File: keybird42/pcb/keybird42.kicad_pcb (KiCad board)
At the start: 2 copper layers, 180 parts, among them SW111 SW_MX, SW112 SW_MX, SW113 SW_MX, SW114 SW_MX, SW115 SW_MX, SW116 SW_MX, SW117 SW_MX, SW121 SW_MX, SW122 SW_MX, SW123 SW_MX, SW124 SW_MX, SW125 SW_MX, SW126 SW_MX, SW127 SW_MX, SW131 SW_MX, SW132 SW_MX, SW133 SW_MX, SW134 SW_MX, SW135 SW_MX, SW136 SW_MX, SW137 SW_MX, SW211 SW_MX, SW212 SW_MX, SW213 SW_MX, SW214 SW_MX, SW215 SW_MX, SW216 SW_MX, SW217 SW_MX, SW221 SW_MX, SW222 SW_MX, SW223 SW_MX, SW225 SW_MX, SW226 SW_MX, SW227 SW_MX, SW231 SW_MX, SW232 SW_MX, SW233 SW_MX, SW234 SW_MX, SW235 SW_MX, SW236 SW_MX, SW237 SW_MX, SW311 SW_MX, SW312 SW_MX, SW313 SW_MX, SW314 SW_MX, SW315 SW_MX, SW316 SW_MX, SW317 SW_MX, SW321 SW_MX, SW322 SW_MX, SW323 SW_MX, SW324 SW_MX, SW325 SW_MX, SW326 SW_MX, SW327 SW_MX, SW331 SW_MX, SW332 SW_MX, SW333 SW_MX, SW334 SW_MX, SW335 SW_MX, SW336 SW_MX, SW337 SW_MX, SW411 SW_MX, SW412 SW_MX, SW413 SW_MX, SW414 SW_MX, SW415 SW_MX, SW416 SW_MX, SW417 SW_MX, SW421 SW_MX, SW422 SW_MX, SW423 SW_MX, SW424 SW_MX, SW425 SW_MX, SW426 SW_MX, SW427 SW_MX, SW431 SW_MX, SW432 SW_MX, SW433 SW_MX, SW434 SW_MX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

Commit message: row 3, two more gaps
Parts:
- removed D313, D326: 1N4148W, Diode_SMD:D_SOD-123
- removed SW313, SW326: SW_MX, PCM_Switch_Keyboard_Hotswap_Kailh:SW_Hotswap_Kailh_MX
- moved SW327 307.4 mm to (406.4, 76.2)
- moved SW316 297.2 mm to (322.6, 63.5)
- moved SW337 283.5 mm to (425.4, 76.2)
- moved SW317 257.9 mm to (387.4, 76.2)
- moved SW315 247.7 mm to (265.4, 63.5)
- moved SW334 240.8 mm to (246.4, 63.5)
- moved SW336 207.5 mm to (348.0, 63.5)
- moved SW333 204.3 mm to (189.2, 63.5)
- moved SW314 203.6 mm to (208.3, 63.5)
- moved SW325 193.7 mm to (284.5, 63.5)
- moved SW332 181.4 mm to (151.1, 63.5)
- moved SW331 163.8 mm to (69.8, 76.2)
- moved SW335 160.5 mm to (303.5, 63.5)
- moved SW312 149.2 mm to (109.2, 63.5)
- moved SW311 146.1 mm to (31.8, 76.2)
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
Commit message: rough positioning of row 4, two more holes
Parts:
- removed D422, D435: 1N4148W, Diode_SMD:D_SOD-123
- removed SW422, SW435: SW_MX, PCM_Switch_Keyboard_Hotswap_Kailh:SW_Hotswap_Kailh_MX
- moved SW437 316.1 mm to (425.4, 95.2)
- moved SW417 281.6 mm to (387.4, 95.2)
- moved SW436 264.4 mm to (361.9, 82.5)
- moved SW427 251.2 mm to (406.4, 95.2)
- moved SW416 219.6 mm to (312.4, 82.5)
- moved SW421 190.8 mm to (50.8, 95.2)
- moved SW426 185.4 mm to (337.8, 82.5)
- moved SW415 181.3 mm to (274.3, 82.5)
- moved SW434 171.2 mm to (255.3, 82.5)
- moved SW425 138.3 mm to (293.4, 82.5)
- moved SW433 134.2 mm to (198.1, 82.5)
- moved SW414 133.8 mm to (217.2, 82.5)
- moved SW411 128.8 mm to (31.8, 95.2)
- moved SW431 128.7 mm to (69.8, 95.2)
- moved SW432 117.1 mm to (141.0, 82.5)
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
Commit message: row 5, no holes, positioning is very sketchy
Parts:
- moved SW507 197.6 mm to (355.6, 101.6)
- moved SW506 167.9 mm to (330.2, 101.6)
- moved SW505 138.2 mm to (304.8, 101.6)
- moved SW501 81.0 mm to (101.6, 101.6)
- moved SW504 67.1 mm to (228.6, 101.6)
- moved SW502 58.3 mm to (127.0, 101.6)
- moved SW503 45.0 mm to (152.4, 101.6)
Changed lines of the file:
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@@
   )
   (footprint "PCM_Switch_Keyboard_Hotswap_Kailh:SW_Hotswap_Kailh_MX" (layer "F.Cu")
-    (at 182.57 134.93)
+    (at 152.4 101.6)
     (descr "Kailh keyswitch Hotswap Socket")
     (tags "Kailh Keyboard Keyswitch Switch Hotswap Socket Relief Cutout")
@@
   )
   (footprint "PCM_Switch_Keyboard_Hotswap_Kailh:SW_Hotswap_Kailh_MX" (layer "F.Cu")
-    (at 182.57 119.38)
+    (at 127 101.6)
     (descr "Kailh keyswitch Hotswap Socket")
     (tags "Kailh Keyboard Keyswitch Switch Hotswap Socket Relief Cutout")
@@
   )
   (footprint "PCM_Switch_Keyboard_Hotswap_Kailh:SW_Hotswap_Kailh_MX" (layer "F.Cu")
-    (at 182.57 150.48)
+    (at 228.6 101.6)
     (descr "Kailh keyswitch Hotswap Socket")
     (tags "Kailh Keyboard Keyswitch Switch Hotswap Socket Relief Cutout")
@@
   )
   (footprint "PCM_Switch_Keyboard_Hotswap_Kailh:SW_Hotswap_Kailh_MX" (layer "F.Cu")
-    (at 182.57 181.58)
+    (at 330.2 101.6)
     (descr "Kailh keyswitch Hotswap Socket")
     (tags "Kailh Keyboard Keyswitch Switch Hotswap Socket Relief Cutout")
@@
   )
   (footprint "PCM_Switch_Keyboard_Hotswap_Kailh:SW_Hotswap_Kailh_MX" (layer "F.Cu")
-    (at 182.57 103.83)
+    (at 101.6 101.6)
     (descr "Kailh keyswitch Hotswap Socket")
     (tags "Kailh Keyboard Keyswitch Switch Hotswap Socket Relief Cutout")
@@
   )
   (footprint "PCM_Switch_Keyboard_Hotswap_Kailh:SW_Hotswap_Kailh_MX" (layer "F.Cu")
-    (at 182.57 197.13)
+    (at 355.6 101.6)
     (descr "Kailh keyswitch Hotswap Socket")
     (tags "Kailh Keyboard Keyswitch Switch Hotswap Socket Relief Cutout")
@@
   )
   (footprint "PCM_Switch_Keyboard_Hotswap_Kailh:SW_Hotswap_Kailh_MX" (layer "F.Cu")
-    (at 182.57 166.03)
+    (at 304.8 101.6)
     (descr "Kailh keyswitch Hotswap Socket")
     (tags "Kailh Keyboard Keyswitch Switch Hotswap Socket Relief Cutout")

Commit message: diodes in roughly the right places
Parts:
- moved D127 279.6 mm to (406.4, 36.8)
- moved D137 275.7 mm to (425.4, 36.8)
- moved D237 273.6 mm to (425.4, 55.9)
- moved D117 249.9 mm to (387.4, 36.8)
- moved D217 249.2 mm to (387.4, 54.6)
- moved D227 245.5 mm to (407.7, 55.9)
- moved D126 239.1 mm to (344.2, 29.2)
- moved D327 238.6 mm to (406.4, 81.3)
- moved D337 237.4 mm to (425.4, 81.3)
- moved D437 234.5 mm to (425.4, 100.3)
- moved D136 228.7 mm to (361.9, 30.5)
- moved D236 223.5 mm to (355.6, 49.5)
- moved D211 221.0 mm to (31.8, 54.6)
- moved D121 215.7 mm to (50.8, 36.8)
- moved D111 212.9 mm to (31.8, 36.8)
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
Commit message: swap pins of switches so that traces to diodes are neater
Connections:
- SW111 pad 1: /COL1 -> Net-(D111-A)
- SW111 pad 2: Net-(D111-A) -> /COL1
- SW112 pad 1: /COL2 -> Net-(D112-A)
- SW112 pad 2: Net-(D112-A) -> /COL2
- SW113 pad 1: /COL3 -> Net-(D113-A)
- SW113 pad 2: Net-(D113-A) -> /COL3
- SW114 pad 1: /COL4 -> Net-(D114-A)
- SW114 pad 2: Net-(D114-A) -> /COL4
- SW115 pad 1: /COL5 -> Net-(D115-A)
- SW115 pad 2: Net-(D115-A) -> /COL5
- SW116 pad 1: /COL6 -> Net-(D116-A)
- SW116 pad 2: Net-(D116-A) -> /COL6
- SW117 pad 1: /COL7 -> Net-(D117-A)
- SW117 pad 2: Net-(D117-A) -> /COL7
- SW121 pad 1: /COL1 -> Net-(D121-A)
- SW121 pad 2: Net-(D121-A) -> /COL1
- SW122 pad 1: /COL2 -> Net-(D122-A)
- SW122 pad 2: Net-(D122-A) -> /COL2
- SW123 pad 1: /COL3 -> Net-(D123-A)
- SW123 pad 2: Net-(D123-A) -> /COL3
- SW124 pad 1: /COL4 -> Net-(D124-A)
- SW124 pad 2: Net-(D124-A) -> /COL4
- SW125 pad 1: /COL5 -> Net-(D125-A)
- SW125 pad 2: Net-(D125-A) -> /COL5
- SW126 pad 1: /COL6 -> Net-(D126-A)
- SW126 pad 2: Net-(D126-A) -> /COL6
- SW127 pad 1: /COL7 -> Net-(D127-A)
- SW127 pad 2: Net-(D127-A) -> /COL7
- SW131 pad 1: /COL1 -> Net-(D131-A)
- SW131 pad 2: Net-(D131-A) -> /COL1
- SW132 pad 1: /COL2 -> Net-(D132-A)
- SW132 pad 2: Net-(D132-A) -> /COL2
- SW133 pad 1: /COL3 -> Net-(D133-A)
- SW133 pad 2: Net-(D133-A) -> /COL3
- SW134 pad 1: /COL4 -> Net-(D134-A)
- SW134 pad 2: Net-(D134-A) -> /COL4
- SW135 pad 1: /COL5 -> Net-(D135-A)
- SW135 pad 2: Net-(D135-A) -> /COL5
- SW136 pad 1: /COL6 -> Net-(D136-A)
- SW136 pad 2: Net-(D136-A) -> /COL6
- SW137 pad 1: /COL7 -> Net-(D137-A)
- SW137 pad 2: Net-(D137-A) -> /COL7
- SW211 pad 1: /COL1 -> Net-(D211-A)
- SW211 pad 2: Net-(D211-A) -> /COL1
- SW212 pad 1: /COL2 -> Net-(D212-A)
- SW212 pad 2: Net-(D212-A) -> /COL2
- SW213 pad 1: /COL3 -> Net-(D213-A)
- SW213 pad 2: Net-(D213-A) -> /COL3
- SW214 pad 1: /COL4 -> Net-(D214-A)
- SW214 pad 2: Net-(D214-A) -> /COL4
- SW215 pad 1: /COL5 -> Net-(D215-A)
- SW215 pad 2: Net-(D215-A) -> /COL5
- SW216 pad 1: /COL6 -> Net-(D216-A)
- SW216 pad 2: Net-(D216-A) -> /COL6
- SW217 pad 1: /COL7 -> Net-(D217-A)
- SW217 pad 2: Net-(D217-A) -> /COL7
- SW221 pad 1: /COL1 -> Net-(D221-A)
- SW221 pad 2: Net-(D221-A) -> /COL1
- SW222 pad 1: /COL2 -> Net-(D222-A)
- SW222 pad 2: Net-(D222-A) -> /COL2
- SW223 pad 1: /COL3 -> Net-(D223-A)
- SW223 pad 2: Net-(D223-A) -> /COL3
- SW225 pad 1: /COL5 -> Net-(D225-A)
- SW225 pad 2: Net-(D225-A) -> /COL5
- SW226 pad 1: /COL6 -> Net-(D226-A)
- SW226 pad 2: Net-(D226-A) -> /COL6
- SW227 pad 1: /COL7 -> Net-(D227-A)
- SW227 pad 2: Net-(D227-A) -> /COL7
- SW231 pad 1: /COL1 -> Net-(D231-A)
- SW231 pad 2: Net-(D231-A) -> /COL1
- SW232 pad 1: /COL2 -> Net-(D232-A)
- SW232 pad 2: Net-(D232-A) -> /COL2
- SW233 pad 1: /COL3 -> Net-(D233-A)
- SW233 pad 2: Net-(D233-A) -> /COL3
- SW234 pad 1: /COL4 -> Net-(D234-A)
- SW234 pad 2: Net-(D234-A) -> /COL4
- SW235 pad 1: /COL5 -> Net-(D235-A)
- SW235 pad 2: Net-(D235-A) -> /COL5
- SW236 pad 1: /COL6 -> Net-(D236-A)
- SW236 pad 2: Net-(D236-A) -> /COL6
- SW237 pad 1: /COL7 -> Net-(D237-A)
- SW237 pad 2: Net-(D237-A) -> /COL7
- SW311 pad 1: /COL1 -> Net-(D311-A)
- SW311 pad 2: Net-(D311-A) -> /COL1
- SW312 pad 1: /COL2 -> Net-(D312-A)
- SW312 pad 2: Net-(D312-A) -> /COL2
- SW314 pad 1: /COL4 -> Net-(D314-A)
- SW314 pad 2: Net-(D314-A) -> /COL4
- SW315 pad 1: /COL5 -> Net-(D315-A)
- SW315 pad 2: Net-(D315-A) -> /COL5
- SW316 pad 1: /COL6 -> Net-(D316-A)
- SW316 pad 2: Net-(D316-A) -> /COL6
- SW317 pad 1: /COL7 -> Net-(D317-A)
- SW317 pad 2: Net-(D317-A) -> /COL7
- SW321 pad 1: /COL1 -> Net-(D321-A)
- SW321 pad 2: Net-(D321-A) -> /COL1
- SW322 pad 1: /COL2 -> Net-(D322-A)
- SW322 pad 2: Net-(D322-A) -> /COL2
- SW323 pad 1: /COL3 -> Net-(D323-A)
- SW323 pad 2: Net-(D323-A) -> /COL3
- SW324 pad 1: /COL4 -> Net-(D324-A)
- SW324 pad 2: Net-(D324-A) -> /COL4
- SW325 pad 1: /COL5 -> Net-(D325-A)
- SW325 pad 2: Net-(D325-A) -> /COL5
- SW327 pad 1: /COL7 -> Net-(D327-A)
- SW327 pad 2: Net-(D327-A) -> /COL7
- SW331 pad 1: /COL1 -> Net-(D331-A)
- SW331 pad 2: Net-(D331-A) -> /COL1
- SW332 pad 1: /COL2 -> Net-(D332-A)
- SW332 pad 2: Net-(D332-A) -> /COL2
- SW333 pad 1: /COL3 -> Net-(D333-A)
- SW333 pad 2: Net-(D333-A) -> /COL3
- SW334 pad 1: /COL4 -> Net-(D334-A)
- SW334 pad 2: Net-(D334-A) -> /COL4
- SW335 pad 1: /COL5 -> Net-(D335-A)
- SW335 pad 2: Net-(D335-A) -> /COL5
- SW336 pad 1: /COL6 -> Net-(D336-A)
- SW336 pad 2: Net-(D336-A) -> /COL6
- SW337 pad 1: /COL7 -> Net-(D337-A)
- SW337 pad 2: Net-(D337-A) -> /COL7
- SW411 pad 1: /COL1 -> Net-(D411-A)
- SW411 pad 2: Net-(D411-A) -> /COL1
- SW412 pad 1: /COL2 -> Net-(D412-A)
- SW412 pad 2: Net-(D412-A) -> /COL2
- SW413 pad 1: /COL3 -> Net-(D413-A)
- SW413 pad 2: Net-(D413-A) -> /COL3
- SW414 pad 1: /COL4 -> Net-(D414-A)
- SW414 pad 2: Net-(D414-A) -> /COL4
- SW415 pad 1: /COL5 -> Net-(D415-A)
- SW415 pad 2: Net-(D415-A) -> /COL5
- SW416 pad 1: /COL6 -> Net-(D416-A)
- SW416 pad 2: Net-(D416-A) -> /COL6
- SW417 pad 1: /COL7 -> Net-(D417-A)
- SW417 pad 2: Net-(D417-A) -> /COL7
- SW421 pad 1: /COL1 -> Net-(D421-A)
- SW421 pad 2: Net-(D421-A) -> /COL1
- SW423 pad 1: /COL3 -> Net-(D423-A)
- SW423 pad 2: Net-(D423-A) -> /COL3
- SW424 pad 1: /COL4 -> Net-(D424-A)
- SW424 pad 2: Net-(D424-A) -> /COL4
- SW425 pad 1: /COL5 -> Net-(D425-A)
- SW425 pad 2: Net-(D425-A) -> /COL5
- SW426 pad 1: /COL6 -> Net-(D426-A)
- SW426 pad 2: Net-(D426-A) -> /COL6
- SW427 pad 1: /COL7 -> Net-(D427-A)
- SW427 pad 2: Net-(D427-A) -> /COL7
- SW431 pad 1: /COL1 -> Net-(D431-A)
- SW431 pad 2: Net-(D431-A) -> /COL1
- SW432 pad 1: /COL2 -> Net-(D432-A)
- SW432 pad 2: Net-(D432-A) -> /COL2
- SW433 pad 1: /COL3 -> Net-(D433-A)
- SW433 pad 2: Net-(D433-A) -> /COL3
- SW434 pad 1: /COL4 -> Net-(D434-A)
- SW434 pad 2: Net-(D434-A) -> /COL4
- SW436 pad 1: /COL6 -> Net-(D436-A)
- SW436 pad 2: Net-(D436-A) -> /COL6
- SW437 pad 1: /COL7 -> Net-(D437-A)
- SW437 pad 2: Net-(D437-A) -> /COL7
- SW501 pad 1: /COL1 -> Net-(D501-A)
- SW501 pad 2: Net-(D501-A) -> /COL1
- SW502 pad 1: /COL2 -> Net-(D502-A)
- SW502 pad 2: Net-(D502-A) -> /COL2
- SW503 pad 1: /COL3 -> Net-(D503-A)
- SW503 pad 2: Net-(D503-A) -> /COL3
- SW504 pad 1: /COL4 -> Net-(D504-A)
- SW504 pad 2: Net-(D504-A) -> /COL4
- SW505 pad 1: /COL5 -> Net-(D505-A)
- SW505 pad 2: Net-(D505-A) -> /COL5
- SW506 pad 1: /COL6 -> Net-(D506-A)
- SW506 pad 2: Net-(D506-A) -> /COL6
- SW507 pad 1: /COL7 -> Net-(D507-A)
- SW507 pad 2: Net-(D507-A) -> /COL7

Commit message: move diodes to back and flip them
done by editing the libraries
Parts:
- D111, D112, D113, D114, D115, D116, D117, D121, D122, D123, D124, D125, D126, D127, D131, D132, D133, D134, D135, D136, D137, D211, D212, D213, D214, D215, D216, D217, D221, D222, D223, D225, D226, D227, D231, D232, D233, D234, D235, D236, D237, D311, D312, D314, D315, D316, D317, D321, D322, D323, D324, D325, D327, D331, D332, D333, D334, D335, D336, D337, D411, D412, D413, D414, D415, D416, D417, D421, D423, D424, D425, D426, D427, D431, D432, D433, D434, D436, D437, D501, D502, D503, D504, D505, D506, D507: footprint Diode_SMD:D_SOD-123 -> keybird42:D_1206_HandSolder_Back

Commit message: hook up per-switch diodes / traces / vias
and make sure they are in correct relative position

absolute positions are still wrong
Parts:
- moved D227 1.80 mm to (406.4, 54.6)
- moved D335 1.80 mm to (303.5, 67.3)
- moved D503 1.80 mm to (152.4, 105.4)
- moved D112 1.80 mm to (95.2, 29.2)
- moved D506 1.80 mm to (330.2, 105.4)
- moved D215 1.80 mm to (256.5, 48.3)
- moved D415 1.80 mm to (274.3, 86.4)
- moved D126 1.27 mm to (342.9, 29.2)
- moved D214 1.27 mm to (218.4, 48.3)
- moved D504 1.27 mm to (228.6, 105.4)
- moved D507 1.27 mm to (355.6, 105.4)
- moved D212 1.27 mm to (101.6, 48.3)
- moved D213 1.27 mm to (161.3, 48.3)
- moved D216 1.27 mm to (313.7, 48.3)
- moved D223 1.27 mm to (180.3, 48.3)
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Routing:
- net /COL1: track 0.00 -> 31.4 mm, vias 0 -> 13
- net /COL7: track 0.00 -> 31.4 mm, vias 0 -> 13
- net /COL5: track 0.00 -> 29.0 mm, vias 0 -> 12
- net /COL3: track 0.00 -> 29.0 mm, vias 0 -> 12
- net /COL6: track 0.00 -> 29.0 mm, vias 0 -> 12
- net /COL2: track 0.00 -> 29.0 mm, vias 0 -> 12
- net /COL4: track 0.00 -> 29.0 mm, vias 0 -> 12
- net /ROW50: track 0.00 -> 11.8 mm, vias 0 -> 7
- net /ROW41: track 0.00 -> 11.8 mm, vias 0 -> 7
- net /ROW33: track 0.00 -> 11.8 mm, vias 0 -> 7
- net /ROW23: track 0.00 -> 11.8 mm, vias 0 -> 7
- net /ROW21: track 0.00 -> 11.8 mm, vias 0 -> 7
- net /ROW13: track 0.00 -> 11.8 mm, vias 0 -> 7
- net /ROW12: track 0.00 -> 11.8 mm, vias 0 -> 7
- net /ROW11: track 0.00 -> 11.8 mm, vias 0 -> 7
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
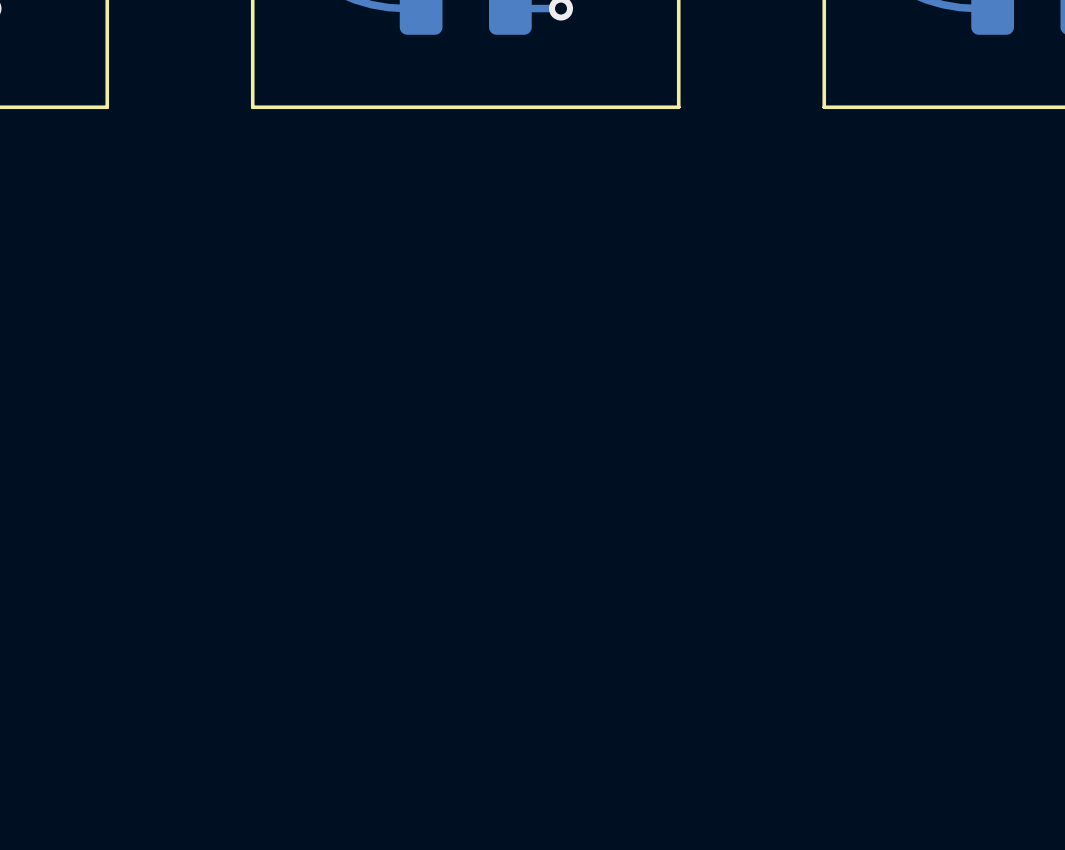
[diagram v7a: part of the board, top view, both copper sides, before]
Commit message: add a footprint for the RP2040-Tiny
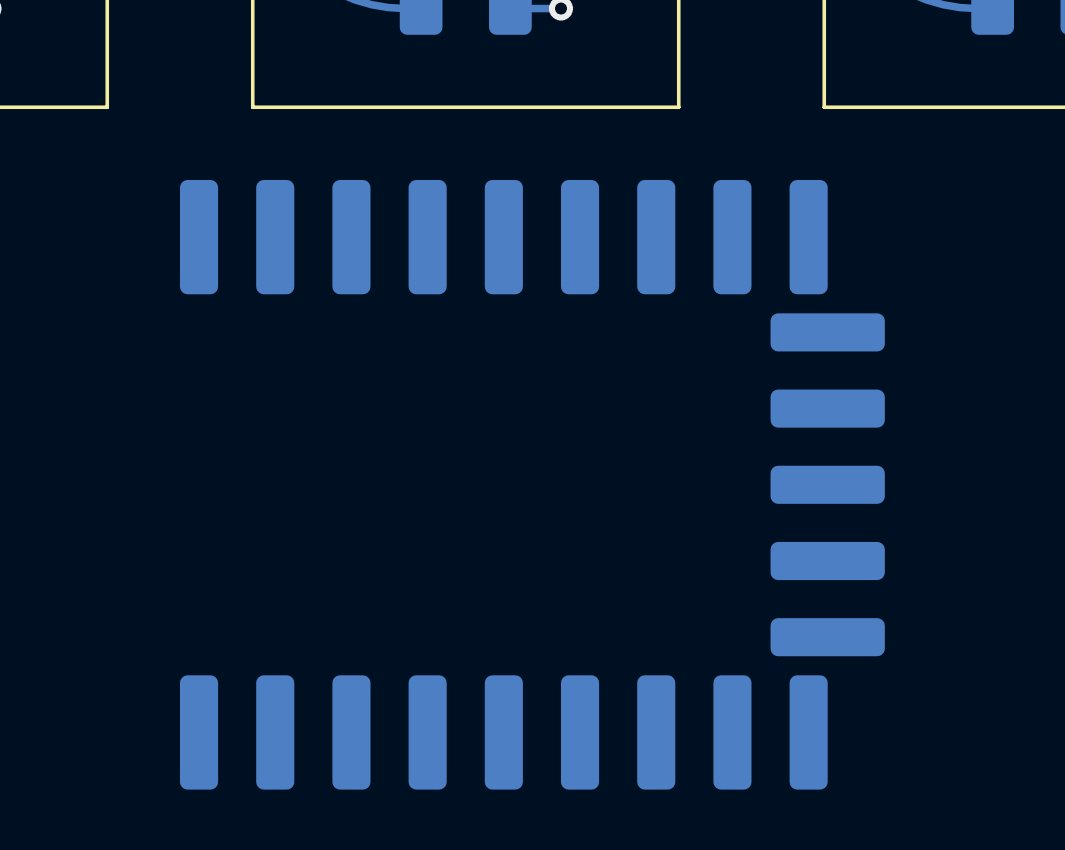
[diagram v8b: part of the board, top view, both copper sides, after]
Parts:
- added U1: RP2040-Tiny, keybird42:RP2040-Tiny, F.Cu at (199.4, 102.2)
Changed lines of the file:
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@@
   (net 105 "/COL6")
   (net 106 "/COL7")
+  (net 107 "unconnected-(U1-3v3-Pad20)")
+  (net 108 "GND")
+  (net 109 "unconnected-(U1-5v-Pad22)")
   (footprint "keybird42:D_1206_HandSolder_Back" (layer "F.Cu")
     (at 228.6 105.41)
@@
     )
   )
+  (footprint "keybird42:RP2040-Tiny" (layer "F.Cu")
+    (at 199.39 102.235)
+    (property "Sheetfile" "keybird42.kicad_sch")
+    (property "Sheetname" "")
+    (property "ki_description" "Waveshare RP2040-Tiny")
+    (property "ki_keywords" "MCU RP2040 raspberrypi")
+    (attr smd)
+    (fp_text reference "U1" (at 0 -0.5 unlocked) (layer "B.SilkS")
+        (effects (font (size 1 1) (thickness 0.1)))
+    )
+    (fp_text value "RP2040-Tiny" (at 0 1 unlocked) (layer "B.SilkS")
+        (effects (font (size 1 1) (thickness 0.15)))
+    )
+    (fp_text user "${REFERENCE}" (at 0 2.5 unlocked) (layer "F.Fab")
+        (effects (font (size 1 1) (thickness 0.15)))
+    )
+    (fp_line (start -8.255 5.08) (end -6.985 5.08)
+      (stroke (width 0.1) (type default)) (layer "B.SilkS"))
+    (fp_line (start -8.128 4.826) (end -7.112 4.826)
+      (stroke (width 0.1) (type default)) (layer "B.SilkS"))
+    (fp_line (start -7.874 4.572) (end -7.366 4.572)
+      (stroke (width 0.1) (type default)) (layer "B.SilkS"))
+    (fp_line (start -7.62 5.715) (end -7.62 5.08)
+      (stroke (width 0.1) (type default)) (layer "B.SilkS"))
+    (fp_rect (start -11.75 -9) (end 11.75 9)
+      (stroke (width 0.1) (type default)) (fill none) (layer "B.SilkS"))
+    (fp_circle (center -10.16 -5.08) (end -9.525 -5.08)
+      (stroke (width 0.1) (type solid)) (fill solid) (layer "B.SilkS"))
+    (pad "0" smd roundrect (at -10.16 -8.255) (size 1.27 3.81) (layers "B.Cu" "B.Paste" "B.Mask") (roundrect_rratio 0.2)
+      (net 1 "/ROW11") (pinfunction "GPIO0") (pintype "bidirectional"))
+    (pad "1" smd roundrect (at -7.62 -8.255) (size 1.27 3.81) (layers "B.Cu" "B.Paste" "B.Mask") (roundrect_rratio 0.2)
+      (net 9 "/ROW12") (pinfunction "GPIO1") (pintype "bidirectional"))
+    (pad "2" smd roundrect (at -5.08 -8.255) (size 1.27 3.81) (layers "B.Cu" "B.Paste" "B.Mask") (roundrect_rratio 0.2)
+      (net 17 "/ROW13") (pinfunction "GPIO2") (pintype "bidirectional"))
+    (pad "3" smd roundrect (at -2.54 -8.255) (size 1.27 3.81) (layers "B.Cu" "B.Paste" "B.Mask") (roundrect_rratio 0.2)
+      (net 25 "/ROW21") (pinfunction "GPIO3") (pintype "bidirectional"))
+    (pad "4" smd roundrect (at 0 -8.255) (size 1.27 3.81) (layers "B.Cu" "B.Paste" "B.Mask") (roundrect_rratio 0.2)
+      (net 33 "/ROW22") (pinfunction "GPIO4") (pintype "bidirectional"))
+    (pad "5" smd roundrect (at 2.54 -8.255) (size 1.27 3.81) (layers "B.Cu" "B.Paste" "B.Mask") (roundrect_rratio 0.2)
+      (net 40 "/ROW23") (pinfunction "GPIO5") (pintype "bidirectional"))
+    (pad "6" smd roundrect (at 5.08 -8.255) (size 1.27 3.81) (layers "B.Cu" "B.Paste" "B.Mask") (roundrect_rratio 0.2)
+      (net 48 "/ROW31") (pinfunction "GPIO6") (pintype "bidirectional"))
+    (pad "7" smd roundrect (at 7.62 -8.255) (size 1.27 3.81) (layers "B.Cu" "B.Paste" "B.Mask") (roundrect_rratio 0.2)
+      (net 56 "/ROW32") (pinfunction "GPIO7") (pintype "bidirectional"))
+    (pad "8" smd roundrect (at 10.16 -8.255) (size 1.27 3.81) (layers "B.Cu" "B.Paste" "B.Mask") (roundrect_rratio 0.2)
+      (net 63 "/ROW33") (pinfunction "GPIO8") (pintype "bidirectional"))
+    (pad "9" smd roundrect (at 10.795 -5.08 90) (size 1.27 3.81) (layers "B.Cu" "B.Paste" "B.Mask") (roundrect_rratio 0.2)
+      (net 71 "/ROW41") (pinfunction "GPIO9") (pintype "bidirectional"))
+    (pad "10" smd roundrect (at 10.795 -2.54 90) (size 1.27 3.81) (layers "B.Cu" "B.Paste" "B.Mask") (roundrect_rratio 0.2)
+      (net 79 "/ROW42") (pinfunction "GPIO10") (pintype "bidirectional"))
+    (pad "11" smd roundrect (at 10.795 0 90) (size 1.27 3.81) (layers "B.Cu" "B.Paste" "B.Mask") (roundrect_rratio 0.2)
+      (net 86 "/ROW43") (pinfunction "GPIO11") (pintype "bidirectional"))
+    (pad "12" smd roundrect (at 10.795 2.54 90) (size 1.27 3.81) (layers "B.Cu" "B.Paste" "B.Mask") (roundrect_rratio 0.2)
+      (net 92 "/ROW50") (pinfunction "GPIO12") (pintype "bidirectional"))
+    (pad "13" smd roundrect (at 10.795 5.08 90) (size 1.27 3.81) (layers "B.Cu" "B.Paste" "B.Mask") (roundrect_rratio 0.2)
+      (net 100 "/COL1") (pinfunction "GPIO13") (pintype "bidirectional"))
+    (pad "14" smd roundrect (at 10.16 8.255 180) (size 1.27 3.81) (layers "B.Cu" "B.Paste" "B.Mask") (roundrect_rratio 0.2)
+      (net 101 "/COL2") (pinfunction "GPIO14") (pintype "bidirectional"))
+    (pad "15" smd roundrect (at 7.62 8.255 180) (size 1.27 3.81) (layers "B.Cu" "B.Paste" "B.Mask") (roundrect_rratio 0.2)
+      (net 102 "/COL3") (pinfunction "GPIO15") (pintype "bidirectional"))
+    (pad "16" smd roundrect (at 5.08 8.255 180) (size 1.27 3.81) (layers "B.Cu" "B.Paste" "B.Mask") (roundrect_rratio 0.2)
+      (net 103 "/COL4") (pinfunction "GPIO26") (pintype "bidirectional"))
+    (pad "17" smd roundrect (at 2.54 8.255 180) (size 1.27 3.81) (layers "B.Cu" "B.Paste" "B.Mask") (roundrect_rratio 0.2)
+      (net 104 "/COL5") (pinfunction "GPIO27") (pintype "bidirectional"))
+    (pad "18" smd roundrect (at 0 8.255 180) (size 1.27 3.81) (layers "B.Cu" "B.Paste" "B.Mask") (roundrect_rratio 0.2)
+      (net 105 "/COL6") (pinfunction "GPIO28") (pintype "bidirectional"))
+    (pad "19" smd roundrect (at -2.54 8.255 180) (size 1.27 3.81) (layers "B.Cu" "B.Paste" "B.Mask") (roundrect_rratio 0.2)
+      (net 106 "/COL7") (pinfunction "GPIO29") (pintype "bidirectional"))
+    (pad "20" smd roundrect (at -5.08 8.255 180) (size 1.27 3.81) (layers "B.Cu" "B.Paste" "B.Mask") (roundrect_rratio 0.2)
+      (net 107 "unconnected-(U1-3v3-Pad20)") (pinfunction "3v3") (pintype "power_out+no_connect"))
+    (pad "21" smd roundrect (at -7.62 8.255 180) (size 1.27 3.81) (layers "B.Cu" "B.Paste" "B.Mask") (roundrect_rratio 0.2)
+      (net 108 "GND") (pinfunction "GND") (pintype "power_out"))
+    (pad "22" smd roundrect (at -10.16 8.255 180) (size 1.27 3.81) (layers "B.Cu" "B.Paste" "B.Mask") (roundrect_rratio 0.2)
+      (net 109 "unconnected-(U1-5v-Pad22)") (pinfunction "5v") (pintype "power_out+no_connect"))
+  )
   (footprint "keybird42:D_1206_HandSolder_Back" (layer "F.Cu")
